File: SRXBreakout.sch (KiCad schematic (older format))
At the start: 23 parts, among them J1 Conn_02x05_Odd_Even, J2 Conn_02x04_Odd_Even

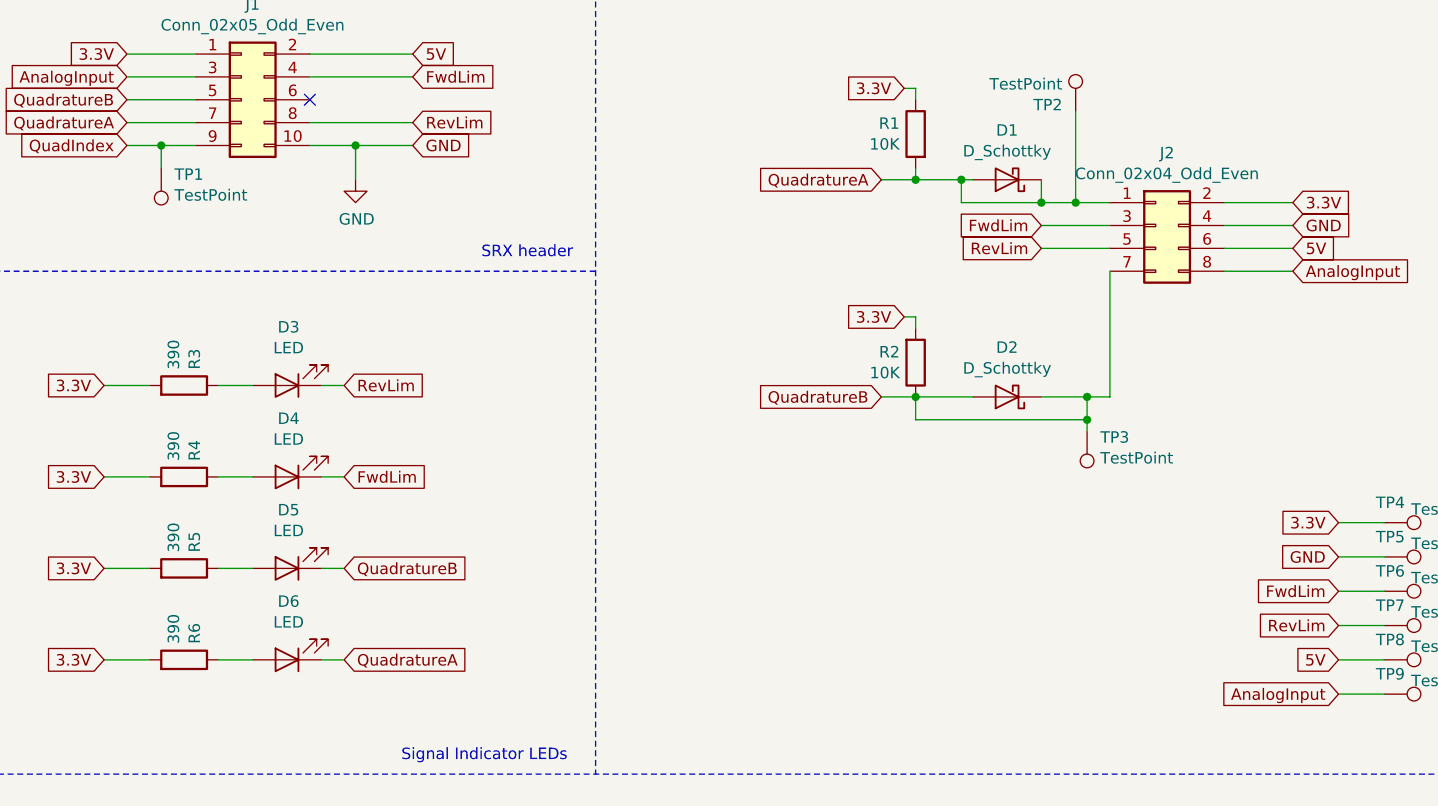
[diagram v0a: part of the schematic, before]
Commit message: added manufacturing files. Updated schematic with as built component values
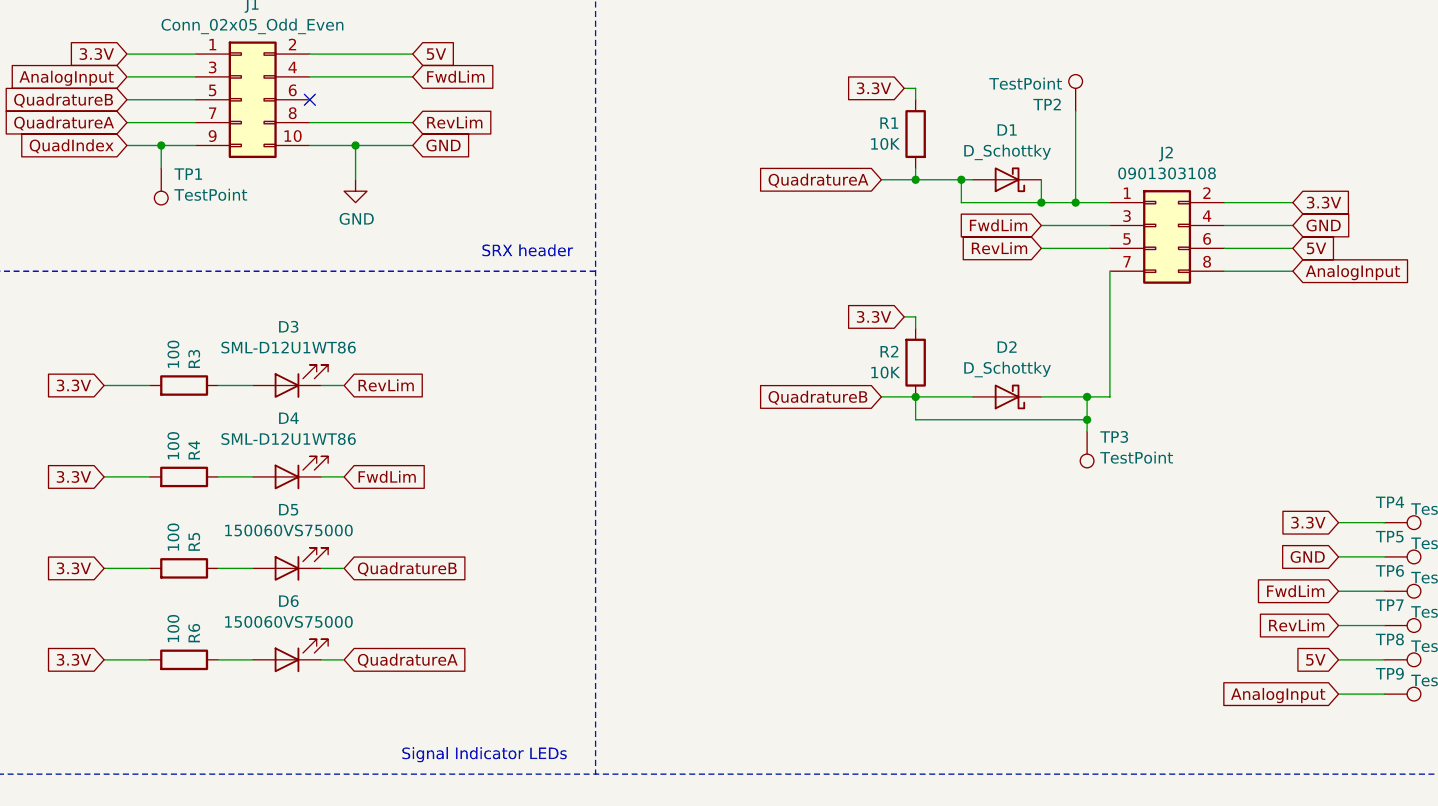
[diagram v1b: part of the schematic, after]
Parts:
- D3, D4: value LED -> SML-D12U1WT86
- D5, D6: value LED -> 150060VS75000
- J2: value Conn_02x04_Odd_Even -> 0901303108
- R3, R4, R5, R6: value 390 -> 100
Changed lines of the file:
@@
 P 8600 3800
 F 0 "J2" H 8650 4117 50  0000 C CNN
-F 1 "Conn_02x04_Odd_Even" H 8650 4026 50  0000 C CNN
+F 1 "0901303108" H 8650 4026 50  0000 C CNN
 F 2 "Connector_PinHeader_2.54mm:PinHeader_2x04_P2.54mm_Vertical_SMD" H 8600 3800 50  0001 C CNN
 F 3 "~" H 8600 3800 50  0001 C CNN
@@
 P 4350 4500
 F 0 "R3" H 4420 4546 50  0000 L CNN
-F 1 "390" H 4420 4455 50  0000 L CNN
+F 1 "100" H 4420 4455 50  0000 L CNN
 F 2 "Resistor_SMD:R_0603_1608Metric_Pad1.05x0.95mm_HandSolder" V 4280 4500 50  0001 C CNN
 F 3 "~" H 4350 4500 50  0001 C CNN
@@
 P 4800 4500
 F 0 "D3" H 4793 4245 50  0000 C CNN
-F 1 "LED" H 4793 4336 50  0000 C CNN
+F 1 "SML-D12U1WT86" H 4793 4336 50  0000 C CNN
 F 2 "Diode_SMD:D_0603_1608Metric_Pad1.05x0.95mm_HandSolder" H 4800 4500 50  0001 C CNN
 F 3 "~" H 4800 4500 50  0001 C CNN
@@
 P 4350 4900
 F 0 "R4" H 4420 4946 50  0000 L CNN
-F 1 "390" H 4420 4855 50  0000 L CNN
+F 1 "100" H 4420 4855 50  0000 L CNN
 F 2 "Resistor_SMD:R_0603_1608Metric_Pad1.05x0.95mm_HandSolder" V 4280 4900 50  0001 C CNN
 F 3 "~" H 4350 4900 50  0001 C CNN
@@
 P 4800 4900
 F 0 "D4" H 4793 4645 50  0000 C CNN
-F 1 "LED" H 4793 4736 50  0000 C CNN
+F 1 "SML-D12U1WT86" H 4793 4736 50  0000 C CNN
 F 2 "Diode_SMD:D_0603_1608Metric_Pad1.05x0.95mm_HandSolder" H 4800 4900 50  0001 C CNN
 F 3 "~" H 4800 4900 50  0001 C CNN
@@
 P 4350 5300
 F 0 "R5" H 4420 5346 50  0000 L CNN
-F 1 "390" H 4420 5255 50  0000 L CNN
+F 1 "100" H 4420 5255 50  0000 L CNN
 F 2 "Resistor_SMD:R_0603_1608Metric_Pad1.05x0.95mm_HandSolder" V 4280 5300 50  0001 C CNN
 F 3 "~" H 4350 5300 50  0001 C CNN
@@
 P 4800 5300
 F 0 "D5" H 4793 5045 50  0000 C CNN
-F 1 "LED" H 4793 5136 50  0000 C CNN
+F 1 "150060VS75000" H 4793 5136 50  0000 C CNN
 F 2 "Diode_SMD:D_0603_1608Metric_Pad1.05x0.95mm_HandSolder" H 4800 5300 50  0001 C CNN
 F 3 "~" H 4800 5300 50  0001 C CNN
@@
 P 4350 5700
 F 0 "R6" H 4420 5746 50  0000 L CNN
-F 1 "390" H 4420 5655 50  0000 L CNN
+F 1 "100" H 4420 5655 50  0000 L CNN
 F 2 "Resistor_SMD:R_0603_1608Metric_Pad1.05x0.95mm_HandSolder" V 4280 5700 50  0001 C CNN
 F 3 "~" H 4350 5700 50  0001 C CNN
@@
 P 4800 5700
 F 0 "D6" H 4793 5445 50  0000 C CNN
-F 1 "LED" H 4793 5536 50  0000 C CNN
+F 1 "150060VS75000" H 4793 5536 50  0000 C CNN
 F 2 "Diode_SMD:D_0603_1608Metric_Pad1.05x0.95mm_HandSolder" H 4800 5700 50  0001 C CNN
 F 3 "~" H 4800 5700 50  0001 C CNN
